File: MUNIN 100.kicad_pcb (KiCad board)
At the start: 2 copper layers, 100 x 75 mm, 78 parts, among them IC1 ACHS-7123, J1 TX_IN, J2 Conn_Coaxial, J3 Conn_01x03_Male, J4 3-647630-4, Q1 ISS55EP06LMXTSA1, Q2 MRF101AN, Q3 MRF101BN, U1 TL783CKTT, U2 LM358

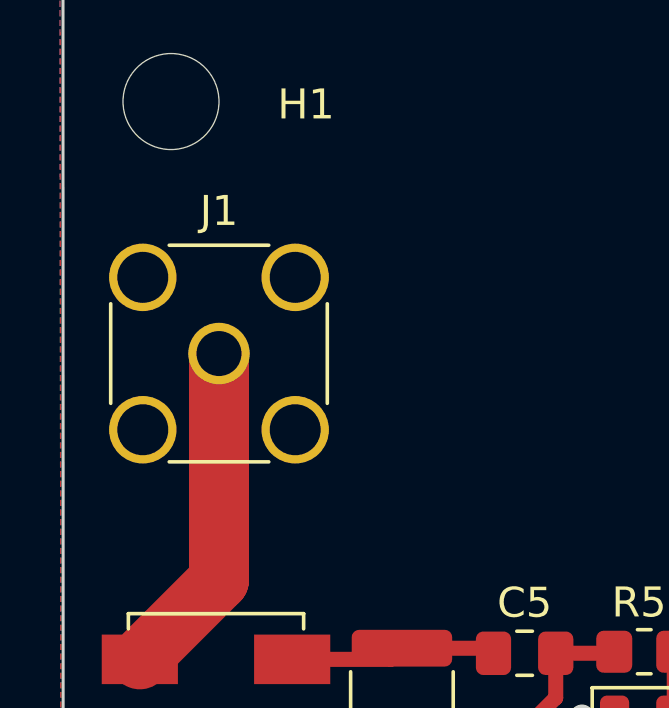
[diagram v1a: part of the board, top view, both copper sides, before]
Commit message: Replaced SMA Conectors
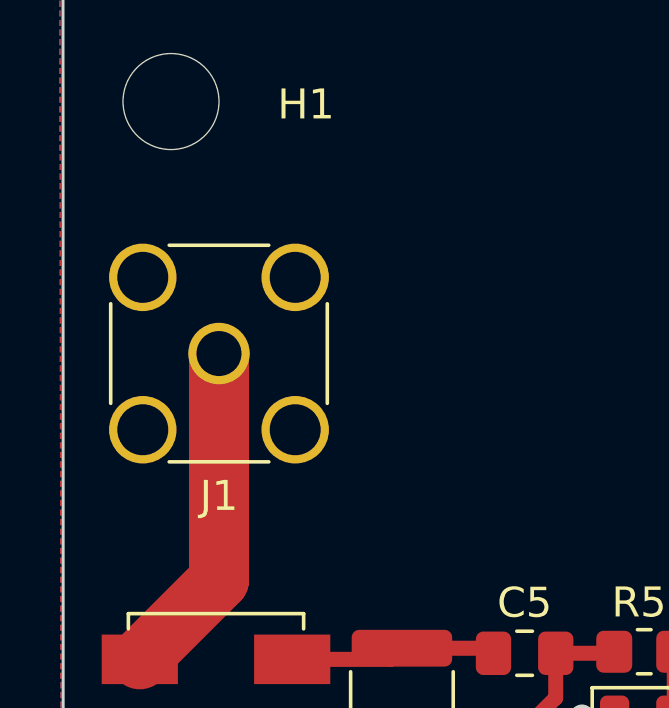
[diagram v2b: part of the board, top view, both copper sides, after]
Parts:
- turned J1 to 180 degrees
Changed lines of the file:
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@@
     (pad "2" thru_hole circle (at 2.54 2.54) (size 2.25 2.25) (drill 1.7) (layers *.Cu *.Mask)
       (net 2 "GND") (pinfunction "Ext") (pintype "passive"))
-    (model "${KICAD6_3DMODEL_DIR}/Connector_Coaxial.3dshapes/SMA_Amphenol_132291_Vertical.step"
-      (offset (xyz 0 0 0))
+    (model "C:/Kicad/Prosjekter/SamacSys_Parts.3dshapes/142-0701-301.stp"
+      (offset (xyz 0 0 6))
       (scale (xyz 1 1 1))
       (rotate (xyz 0 0 0))
@@
   )
   (footprint "Connector_Coaxial:SMA_Amphenol_132291-12_Vertical" (layer "F.Cu")
-    (at 50.9 89.4)
+    (at 50.9 89.4 180)
     (descr "https://www.amphenolrf.com/downloads/dl/file/id/1688/product/3020/132291_12_customer_drawing.pdf")
     (tags "SMA THT Female Jack Vertical Bulkhead")
@@
       (effects (font (size 1 1) (thickness 0.15)))
     )
-    (fp_text value "TX_IN" (at 0 5) (layer "F.Fab")
+    (fp_text value "TX_IN" (at 0.2 -5) (layer "F.Fab")
       (effects (font (size 1 1) (thickness 0.15)))
     )
@@
     (fp_line (start -3.5 3.5) (end 3.5 3.5) (layer "F.Fab") (width 0.1))
     (fp_circle (center 0 0) (end 3.175 0) (layer "F.Fab") (width 0.1) (fill none))
-    (pad "1" thru_hole circle (at 0 0) (size 2.05 2.05) (drill 1.5) (layers *.Cu *.Mask)
+    (pad "1" thru_hole circle (at 0 0 180) (size 2.05 2.05) (drill 1.5) (layers *.Cu *.Mask)
       (net 19 "Net-(J1-Pad1)") (pinfunction "In") (pintype "passive"))
-    (pad "2" thru_hole circle (at 2.54 -2.54) (size 2.25 2.25) (drill 1.7) (layers *.Cu *.Mask)
+    (pad "2" thru_hole circle (at 2.54 -2.54 180) (size 2.25 2.25) (drill 1.7) (layers *.Cu *.Mask)
       (net 2 "GND") (pinfunction "Ext") (pintype "passive"))
-    (pad "2" thru_hole circle (at -2.54 -2.54) (size 2.25 2.25) (drill 1.7) (layers *.Cu *.Mask)
+    (pad "2" thru_hole circle (at -2.54 -2.54 180) (size 2.25 2.25) (drill 1.7) (layers *.Cu *.Mask)
       (net 2 "GND") (pinfunction "Ext") (pintype "passive"))
-    (pad "2" thru_hole circle (at 2.54 2.54) (size 2.25 2.25) (drill 1.7) (layers *.Cu *.Mask)
+    (pad "2" thru_hole circle (at 2.54 2.54 180) (size 2.25 2.25) (drill 1.7) (layers *.Cu *.Mask)
       (net 2 "GND") (pinfunction "Ext") (pintype "passive"))
-    (pad "2" thru_hole circle (at -2.54 2.54) (size 2.25 2.25) (drill 1.7) (layers *.Cu *.Mask)
+    (pad "2" thru_hole circle (at -2.54 2.54 180) (size 2.25 2.25) (drill 1.7) (layers *.Cu *.Mask)
       (net 2 "GND") (pinfunction "Ext") (pintype "passive"))
-    (model "${KICAD6_3DMODEL_DIR}/Connector_Coaxial.3dshapes/SMA_Amphenol_132291_Vertical.step"
-      (offset (xyz 0 0 0))
-      (scale (xyz 1 1 1))
-      (rotate (xyz 0 0 0))
+    (model "C:/Kicad/Prosjekter/SamacSys_Parts.3dshapes/142-0701-301.stp"
+      (offset (xyz 0 0 6))
+      (scale (xyz 1 1 1))
+      (rotate (xyz 0 0 0))

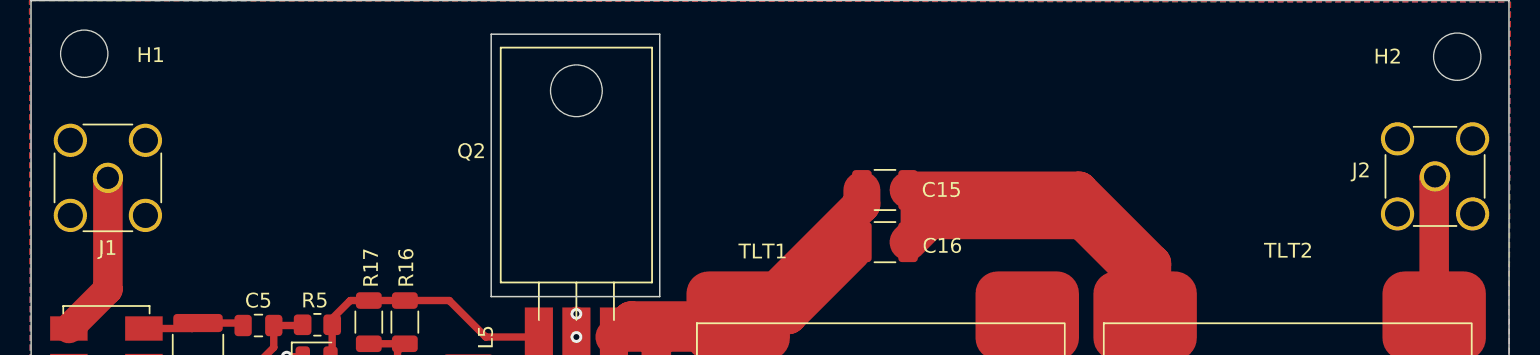
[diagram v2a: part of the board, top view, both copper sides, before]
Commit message: Updated SMA Connectors 3-d
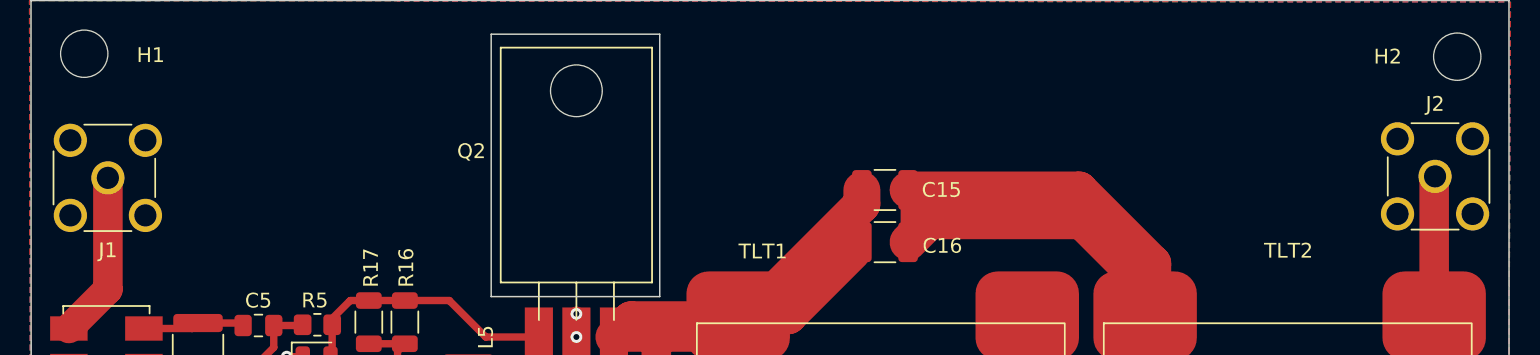
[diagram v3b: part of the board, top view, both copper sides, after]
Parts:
- J1: footprint Connector_Coaxial:SMA_Amphenol_132291-12_Vertical -> Connector_Coaxial:SMA_Molex_73251-2200_Horizontal
- J2: footprint Connector_Coaxial:SMA_Amphenol_132134-11_Vertical -> Connector_Coaxial:SMA_Molex_73251-2200_Horizontal
- turned J1 to 90 degrees
- turned J2 to -90 degrees

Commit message: Added Gerber files
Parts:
- J1, J2: footprint Connector_Coaxial:SMA_Molex_73251-2200_Horizontal -> Connector_Coaxial:SMA_Amphenol_132291_Vertical
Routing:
- net GND: track 52.0 -> 106.1 mm, vias 37 -> 51
- net Net-(D4-Pad2): track 18.9 -> 18.2 mm
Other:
- outline, holes or cut-outs redrawn
- board text added: "RF IN"
- board text added: "RF OUT"
